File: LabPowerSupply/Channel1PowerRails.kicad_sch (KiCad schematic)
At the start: 11 parts

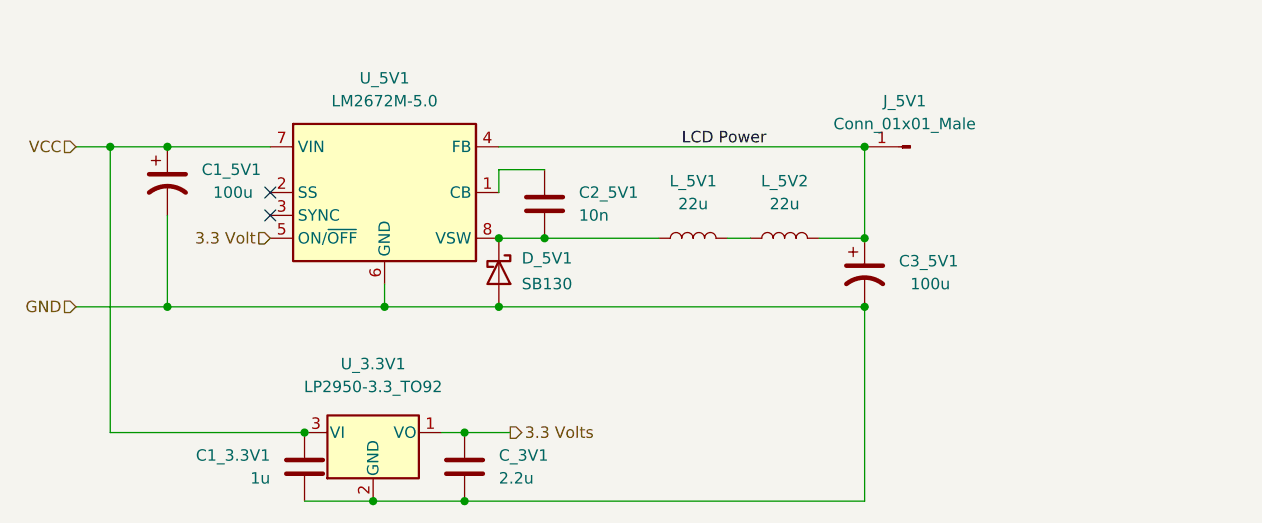
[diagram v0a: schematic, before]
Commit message: Changed most parts to smd
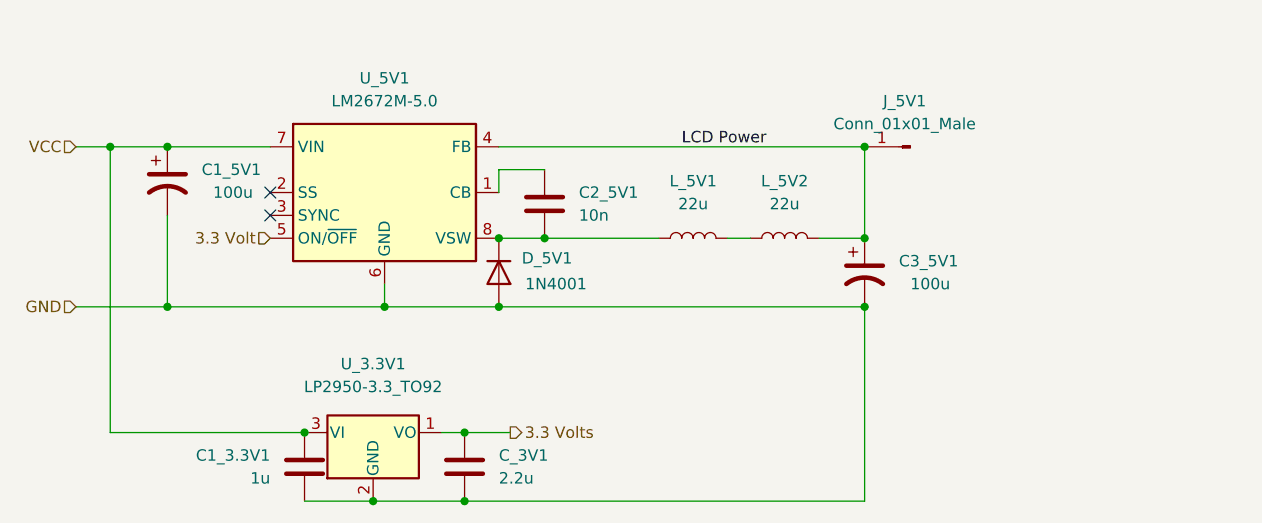
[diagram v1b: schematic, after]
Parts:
- C1_3.3V1, C_3V1: footprint Capacitor_THT:C_Disc_D5.0mm_W2.5mm_P2.50mm -> Capacitor_SMD:C_0805_2012Metric
- C2_5V1: footprint Capacitor_THT:C_Disc_D6.0mm_W2.5mm_P5.00mm -> Capacitor_SMD:C_0805_2012Metric
- D_5V1: value SB130 -> 1N4001; footprint Diode_THT:D_DO-41_SOD81_P10.16mm_Horizontal -> Diode_SMD:D_SMA; symbol Diode:SB130 -> Diode:1N4001
- U_3.3V1: footprint Package_TO_SOT_THT:TO-92_Inline -> Package_TO_SOT_SMD:TO-252-3_TabPin4
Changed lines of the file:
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@@
       (effects (font (size 1.27 1.27)) (justify left))
     )
-    (property "Footprint" "Capacitor_THT:C_Disc_D5.0mm_W2.5mm_P2.50mm" (id 2) (at 136.8552 128.27 0)
+    (property "Footprint" "Capacitor_SMD:C_0805_2012Metric" (id 2) (at 136.8552 128.27 0)
       (effects (font (size 1.27 1.27)) hide)
     )
@@
     (property "Reference" "U_3.3V1" (id 0) (at 125.73 113.03 0))
     (property "Value" "LP2950-3.3_TO92" (id 1) (at 125.73 115.57 0))
-    (property "Footprint" "Package_TO_SOT_THT:TO-92_Inline" (id 2) (at 125.73 114.935 0)
+    (property "Footprint" "Package_TO_SOT_SMD:TO-252-3_TabPin4" (id 2) (at 125.73 114.935 0)
       (effects (font (size 1.27 1.27) italic) hide)
     )
@@
       (effects (font (size 1.27 1.27)) (justify right))
     )
-    (property "Footprint" "Capacitor_THT:C_Disc_D5.0mm_W2.5mm_P2.50mm" (id 2) (at 119.0752 120.65 0)
+    (property "Footprint" "Capacitor_SMD:C_0805_2012Metric" (id 2) (at 119.0752 120.65 0)
       (effects (font (size 1.27 1.27)) hide)
     )
@@
     (pin "2")
   )
-  (symbol (lib_id "Diode:SB130") (at 139.7 102.87 270) (unit 1)
+  (symbol (lib_id "Diode:1N4001") (at 139.7 102.87 270) (unit 1)
     (in_bom yes) (on_board yes)
     (property "Reference" "D_5V1" (id 0) (at 142.24 101.2824 90)
       (effects (font (size 1.27 1.27)) (justify left))
     )
-    (property "Value" "SB130" (id 1) (at 142.24 104.14 90)
-      (effects (font (size 1.27 1.27)) (justify left))
-    )
-    (property "Footprint" "Diode_THT:D_DO-41_SOD81_P10.16mm_Horizontal" (id 2) (at 135.255 102.87 0)
+    (property "Value" "1N4001" (id 1) (at 146.05 104.14 90))
+    (property "Footprint" "Diode_SMD:D_SMA" (id 2) (at 135.255 102.87 0)
       (effects (font (size 1.27 1.27)) hide)
     )
-    (property "Datasheet" "http://www.diodes.com/_files/datasheets/ds23022.pdf" (id 3) (at 139.7 102.87 0)
+    (property "Datasheet" "http://www.vishay.com/docs/88503/1n4001.pdf" (id 3) (at 139.7 102.87 0)
       (effects (font (size 1.27 1.27)) hide)
     )
@@
       (effects (font (size 1.27 1.27)) (justify left))
     )
-    (property "Footprint" "Capacitor_THT:C_Disc_D6.0mm_W2.5mm_P5.00mm" (id 2) (at 145.7452 99.06 0)
+    (property "Footprint" "Capacitor_SMD:C_0805_2012Metric" (id 2) (at 145.7452 99.06 0)
       (effects (font (size 1.27 1.27)) hide)
     )

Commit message: Start tallying
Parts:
- removed D_5V1: 1N4001, Diode_SMD:D_SMA, symbol Diode:1N4001
- removed J_5V1: Conn_01x01_Male, Connector_PinHeader_2.54mm:PinHeader_1x01_P2.54mm_Vertical, symbol Connector:Conn_01x01_Male
- removed L_5V2: 22u, Inductor_THT:L_Radial_D6.0mm_P4.00mm, symbol Device:L
- removed U_5V1: LM2672M-5.0, Package_SO:SOIC-8_3.9x4.9mm_P1.27mm, symbol Regulator_Switching:LM2672M-5.0
- added U_5V1: AP63205WU, Package_TO_SOT_SMD:TSOT-23-6, symbol Regulator_Switching:AP63205WU
- C1_5V1: value 100u -> 10u; footprint Capacitor_THT:CP_Radial_D10.0mm_P5.00mm -> Capacitor_THT:CP_Radial_D8.0mm_P3.50mm
- C2_5V1: value 10n -> 100n; footprint Capacitor_SMD:C_0805_2012Metric -> Capacitor_SMD:C_0603_1608Metric
- C3_5V1: value 100u -> 68u; footprint Capacitor_THT:CP_Radial_D10.0mm_P5.00mm -> Capacitor_THT:CP_Radial_D8.0mm_P3.50mm
- L_5V1: value 22u -> 4.7u; footprint Inductor_THT:L_Radial_D6.0mm_P4.00mm -> Inductor_SMD:L_Sumida_CDMC6D28_7.25x6.5mm
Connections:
- net LCD Power is gone; now on net 5 Volts: C3_5V1.1
- net GND: now also U_5V1.4 (GND)
- net VCC: now also U_5V1.2 (EN), U_5V1.3 (IN)
- net at L_5V1.1: now also C2_5V1.1, U_5V1.5 (SW); no longer C2_5V1.2
- net 5 Volts: now reaches L_5V1.2
- net 5 Volts: now also U_5V1.1 (FB)
- new net: C2_5V1.2, U_5V1.6 (BST)
- no-connect marks 2 -> 0
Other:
- moved on the sheet: C1_3.3V1, C1_5V1, C3_5V1

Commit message: almost done
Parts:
- C1_3.3V1: footprint Capacitor_SMD:C_0805_2012Metric -> Capacitor_SMD:C_0603_1608Metric
- C1_5V1: value 10u -> 68u
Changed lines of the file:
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@@
       (effects (font (size 1.27 1.27)) (justify right))
     )
-    (property "Footprint" "Capacitor_SMD:C_0805_2012Metric" (id 2) (at 111.4552 120.65 0)
+    (property "Footprint" "Capacitor_SMD:C_0603_1608Metric" (id 2) (at 111.4552 120.65 0)
       (effects (font (size 1.27 1.27)) hide)
     )
@@
       (effects (font (size 1.27 1.27)) (justify left))
     )
-    (property "Value" "10u" (id 1) (at 107.95 101.6 0)
+    (property "Value" "68u" (id 1) (at 107.95 101.6 0)
       (effects (font (size 1.27 1.27)) (justify left))
     )

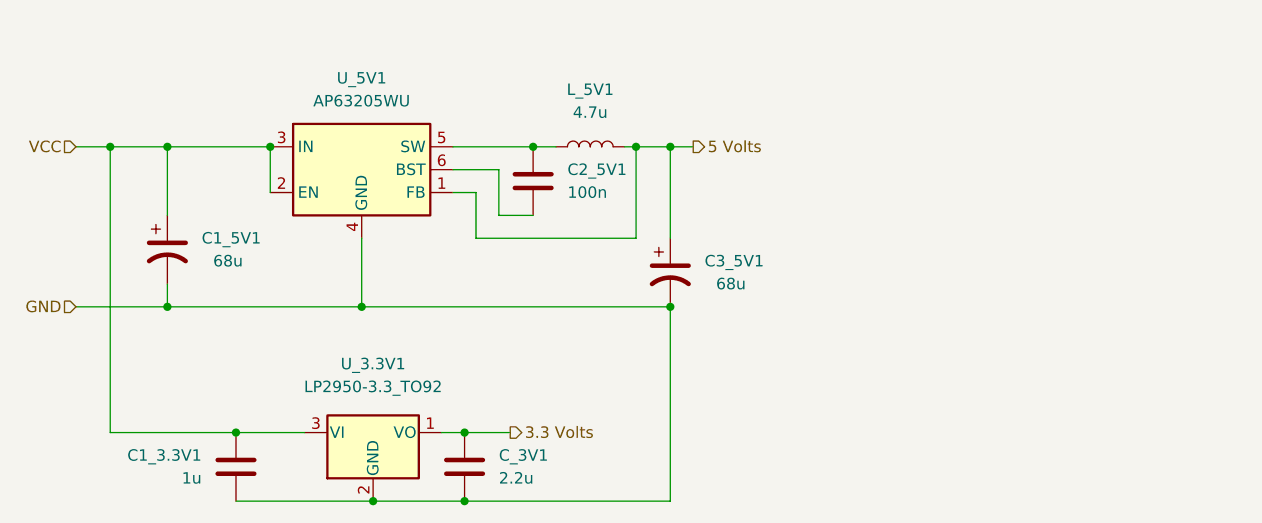
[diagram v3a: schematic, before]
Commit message: Pre regulate 3.3v
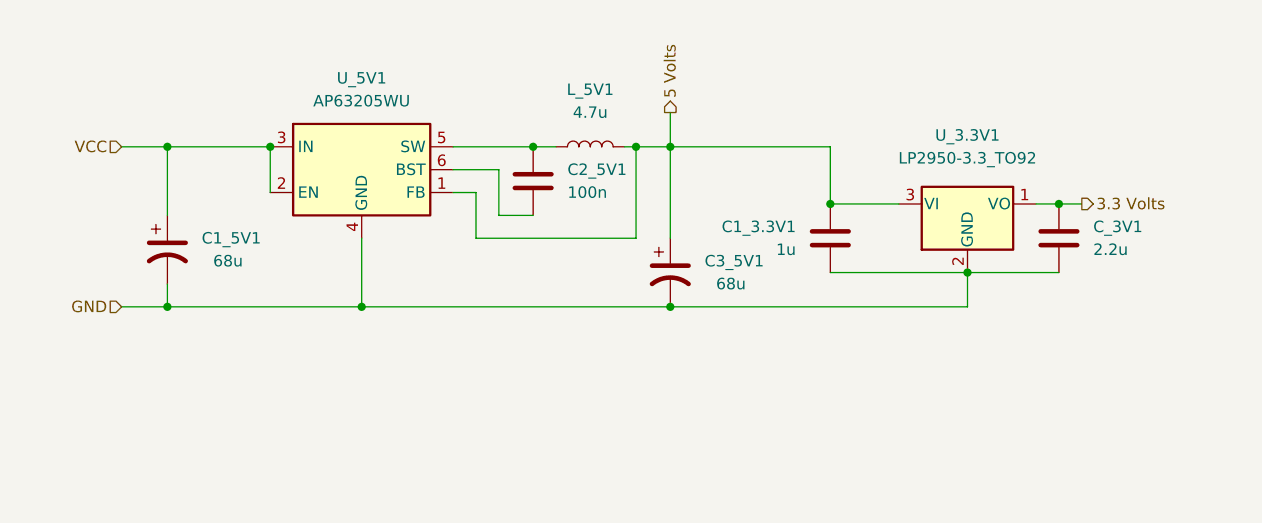
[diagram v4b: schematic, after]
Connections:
- net 5 Volts: now also C1_3.3V1.2, U_3.3V1.3 (VI)
- net VCC: no longer C1_3.3V1.2, U_3.3V1.3 (VI)
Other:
- moved on the sheet: C1_3.3V1, C_3V1, U_3.3V1
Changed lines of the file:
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@@
     (comment 4 "This supplys the 5 volts and 3.3 volts rail for the primary digital")
-  )
-  (junction (at 110.49 120.65) (diameter 0) (color 0 0 0 0)
   )
   (junction (at 102.87 106.68) (diameter 0) (color 0 0 0 0)
@@
   (junction (at 114.3 88.9) (diameter 0) (color 0 0 0 0)
   )
-  (junction (at 96.52 88.9) (diameter 0) (color 0 0 0 0)
-  )
-  (junction (at 135.89 128.27) (diameter 0) (color 0 0 0 0)
+  (junction (at 176.53 95.25) (diameter 0) (color 0 0 0 0)
   )
   (junction (at 158.75 106.68) (diameter 0) (color 0 0 0 0)
   )
+  (junction (at 124.46 106.68) (diameter 0) (color 0 0 0 0)
+  )
+  (junction (at 191.77 102.87) (diameter 0) (color 0 0 0 0)
+  )
   (junction (at 158.75 88.9) (diameter 0) (color 0 0 0 0)
   )
-  (junction (at 124.46 106.68) (diameter 0) (color 0 0 0 0)
-  )
-  (junction (at 125.73 128.27) (diameter 0) (color 0 0 0 0)
-  )
-  (junction (at 135.89 120.65) (diameter 0) (color 0 0 0 0)
+  (junction (at 201.93 95.25) (diameter 0) (color 0 0 0 0)
   )
   (junction (at 143.51 88.9) (diameter 0) (color 0 0 0 0)
@@
     (stroke (width 0) (type default) (color 0 0 0 0))
   )
-  (wire (pts (xy 92.71 88.9) (xy 96.52 88.9))
+  (wire (pts (xy 97.79 88.9) (xy 102.87 88.9))
     (stroke (width 0) (type default) (color 0 0 0 0))
   )
@@
     (stroke (width 0) (type default) (color 0 0 0 0))
   )
-  (wire (pts (xy 110.49 128.27) (xy 125.73 128.27))
+  (wire (pts (xy 201.93 95.25) (xy 204.47 95.25))
     (stroke (width 0) (type default) (color 0 0 0 0))
   )
-  (wire (pts (xy 158.75 128.27) (xy 158.75 106.68))
+  (wire (pts (xy 176.53 102.87) (xy 191.77 102.87))
     (stroke (width 0) (type default) (color 0 0 0 0))
   )
-  (wire (pts (xy 96.52 120.65) (xy 110.49 120.65))
+  (wire (pts (xy 176.53 88.9) (xy 176.53 95.25))
     (stroke (width 0) (type default) (color 0 0 0 0))
   )
@@
     (stroke (width 0) (type default) (color 0 0 0 0))
   )
-  (wire (pts (xy 134.62 88.9) (xy 143.51 88.9))
+  (wire (pts (xy 158.75 88.9) (xy 176.53 88.9))
     (stroke (width 0) (type default) (color 0 0 0 0))
   )
-  (wire (pts (xy 96.52 120.65) (xy 96.52 88.9))
+  (wire (pts (xy 134.62 88.9) (xy 143.51 88.9))
     (stroke (width 0) (type default) (color 0 0 0 0))
   )
@@
     (stroke (width 0) (type default) (color 0 0 0 0))
   )
-  (wire (pts (xy 139.7 91.44) (xy 134.62 91.44))
+  (wire (pts (xy 158.75 85.09) (xy 158.75 88.9))
     (stroke (width 0) (type default) (color 0 0 0 0))
   )
-  (wire (pts (xy 135.89 128.27) (xy 158.75 128.27))
-    (stroke (width 0) (type default) (color 0 0 0 0))
-  )
-  (wire (pts (xy 158.75 88.9) (xy 161.29 88.9))
+  (wire (pts (xy 139.7 91.44) (xy 134.62 91.44))
     (stroke (width 0) (type default) (color 0 0 0 0))
   )
@@
     (stroke (width 0) (type default) (color 0 0 0 0))
   )
-  (wire (pts (xy 96.52 88.9) (xy 102.87 88.9))
+  (wire (pts (xy 158.75 106.68) (xy 191.77 106.68))
     (stroke (width 0) (type default) (color 0 0 0 0))
   )
@@
     (stroke (width 0) (type default) (color 0 0 0 0))
   )
-  (wire (pts (xy 110.49 120.65) (xy 118.11 120.65))
+  (wire (pts (xy 176.53 95.25) (xy 184.15 95.25))
     (stroke (width 0) (type default) (color 0 0 0 0))
   )
@@
     (stroke (width 0) (type default) (color 0 0 0 0))
   )
-  (wire (pts (xy 92.71 106.68) (xy 102.87 106.68))
+  (wire (pts (xy 191.77 106.68) (xy 191.77 102.87))
+    (stroke (width 0) (type default) (color 0 0 0 0))
+  )
+  (wire (pts (xy 97.79 106.68) (xy 102.87 106.68))
     (stroke (width 0) (type default) (color 0 0 0 0))
   )
@@
     (stroke (width 0) (type default) (color 0 0 0 0))
   )
-  (wire (pts (xy 125.73 128.27) (xy 135.89 128.27))
+  (wire (pts (xy 191.77 102.87) (xy 201.93 102.87))
     (stroke (width 0) (type default) (color 0 0 0 0))
   )
@@
     (stroke (width 0) (type default) (color 0 0 0 0))
   )
-  (wire (pts (xy 135.89 120.65) (xy 140.97 120.65))
-    (stroke (width 0) (type default) (color 0 0 0 0))
-  )
   (wire (pts (xy 102.87 106.68) (xy 124.46 106.68))
     (stroke (width 0) (type default) (color 0 0 0 0))
   )
-  (wire (pts (xy 133.35 120.65) (xy 135.89 120.65))
+  (wire (pts (xy 199.39 95.25) (xy 201.93 95.25))
     (stroke (width 0) (type default) (color 0 0 0 0))
   )
@@
     (stroke (width 0) (type default) (color 0 0 0 0))
   )
-  (hierarchical_label "GND" (shape input) (at 92.71 106.68 180)
+  (hierarchical_label "GND" (shape input) (at 97.79 106.68 180)
     (effects (font (size 1.27 1.27)) (justify right))
   )
-  (hierarchical_label "3.3 Volts" (shape output) (at 140.97 120.65 0)
+  (hierarchical_label "3.3 Volts" (shape output) (at 204.47 95.25 0)
     (effects (font (size 1.27 1.27)) (justify left))
   )
-  (hierarchical_label "VCC" (shape input) (at 92.71 88.9 180)
+  (hierarchical_label "VCC" (shape input) (at 97.79 88.9 180)
     (effects (font (size 1.27 1.27)) (justify right))
   )
-  (hierarchical_label "5 Volts" (shape output) (at 161.29 88.9 0)
+  (hierarchical_label "5 Volts" (shape output) (at 158.75 85.09 90)
     (effects (font (size 1.27 1.27)) (justify left))
   )
-  (symbol (lib_id "Device:C") (at 135.89 124.46 0) (unit 1)
+  (symbol (lib_id "Device:C") (at 201.93 99.06 0) (unit 1)
     (in_bom yes) (on_board yes) (fields_autoplaced)
-    (property "Reference" "C_3V1" (id 0) (at 139.7 123.1899 0)
+    (property "Reference" "C_3V1" (id 0) (at 205.74 97.7899 0)
       (effects (font (size 1.27 1.27)) (justify left))
     )
-    (property "Value" "2.2u" (id 1) (at 139.7 125.7299 0)
+    (property "Value" "2.2u" (id 1) (at 205.74 100.3299 0)
       (effects (font (size 1.27 1.27)) (justify left))
     )
-    (property "Footprint" "Capacitor_SMD:C_0805_2012Metric" (id 2) (at 136.8552 128.27 0)
+    (property "Footprint" "Capacitor_SMD:C_0805_2012Metric" (id 2) (at 202.8952 102.87 0)
       (effects (font (size 1.27 1.27)) hide)
     )
-    (property "Datasheet" "~" (id 3) (at 135.89 124.46 0)
+    (property "Datasheet" "~" (id 3) (at 201.93 99.06 0)
       (effects (font (size 1.27 1.27)) hide)
     )
@@
     (pin "2")
   )
-  (symbol (lib_id "Regulator_Linear:LP2950-3.3_TO92") (at 125.73 120.65 0) (unit 1)
+  (symbol (lib_id "Regulator_Linear:LP2950-3.3_TO92") (at 191.77 95.25 0) (unit 1)
     (in_bom yes) (on_board yes) (fields_autoplaced)
-    (property "Reference" "U_3.3V1" (id 0) (at 125.73 113.03 0))
-    (property "Value" "LP2950-3.3_TO92" (id 1) (at 125.73 115.57 0))
-    (property "Footprint" "Package_TO_SOT_SMD:TO-252-3_TabPin4" (id 2) (at 125.73 114.935 0)
+    (property "Reference" "U_3.3V1" (id 0) (at 191.77 87.63 0))
+    (property "Value" "LP2950-3.3_TO92" (id 1) (at 191.77 90.17 0))
+    (property "Footprint" "Package_TO_SOT_SMD:TO-252-3_TabPin4" (id 2) (at 191.77 89.535 0)
       (effects (font (size 1.27 1.27) italic) hide)
     )
-    (property "Datasheet" "http://www.ti.com/lit/ds/symlink/lp2950.pdf" (id 3) (at 125.73 121.92 0)
+    (property "Datasheet" "http://www.ti.com/lit/ds/symlink/lp2950.pdf" (id 3) (at 191.77 96.52 0)
       (effects (font (size 1.27 1.27)) hide)
     )
@@
     (pin "3")
   )
-  (symbol (lib_id "Device:C") (at 110.49 124.46 0) (mirror x) (unit 1)
+  (symbol (lib_id "Device:C") (at 176.53 99.06 0) (mirror x) (unit 1)
     (in_bom yes) (on_board yes) (fields_autoplaced)
-    (property "Reference" "C1_3.3V1" (id 0) (at 106.68 123.1899 0)
+    (property "Reference" "C1_3.3V1" (id 0) (at 172.72 97.7899 0)
       (effects (font (size 1.27 1.27)) (justify right))
     )
-    (property "Value" "1u" (id 1) (at 106.68 125.7299 0)
+    (property "Value" "1u" (id 1) (at 172.72 100.3299 0)
       (effects (font (size 1.27 1.27)) (justify right))
     )
-    (property "Footprint" "Capacitor_SMD:C_0603_1608Metric" (id 2) (at 111.4552 120.65 0)
+    (property "Footprint" "Capacitor_SMD:C_0603_1608Metric" (id 2) (at 177.4952 95.25 0)
       (effects (font (size 1.27 1.27)) hide)
     )
-    (property "Datasheet" "~" (id 3) (at 110.49 124.46 0)
+    (property "Datasheet" "~" (id 3) (at 176.53 99.06 0)
       (effects (font (size 1.27 1.27)) hide)
     )

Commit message: Changed capacitors to x7r
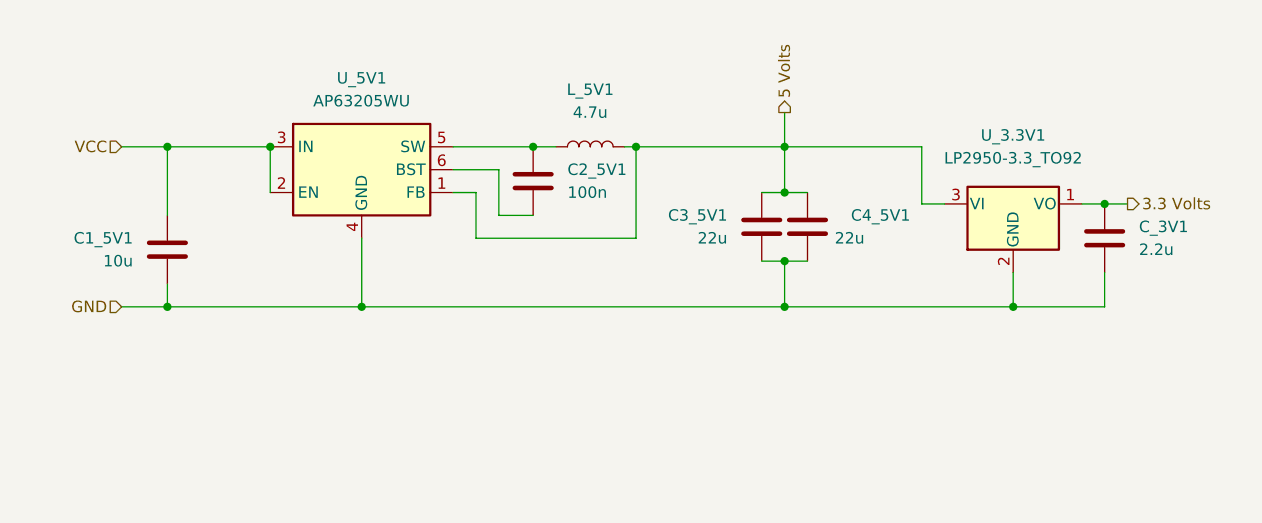
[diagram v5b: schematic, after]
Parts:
- removed C1_3.3V1: 1u, Capacitor_SMD:C_0603_1608Metric, symbol Device:C
- removed C1_5V1, C3_5V1: 68u, Capacitor_THT:CP_Radial_D8.0mm_P3.50mm, symbol Device:C_Polarized_US
- added C1_5V1: 10u, Capacitor_SMD:C_1210_3225Metric, symbol Device:C
- added C3_5V1, C4_5V1: 22u, Capacitor_SMD:C_1210_3225Metric, symbol Device:C
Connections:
- net 5 Volts: now also C3_5V1.2, C4_5V1.2
- net GND: now also C1_5V1.1, C3_5V1.1, C4_5V1.1
- net VCC: now also C1_5V1.2
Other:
- moved on the sheet: C_3V1, U_3.3V1

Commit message: Fixed cap footprints
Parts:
- C1_5V1: footprint Capacitor_SMD:C_1210_3225Metric -> Capacitor_SMD:C_1206_3216Metric
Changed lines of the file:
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@@
       (effects (font (size 1.27 1.27)) (justify right))
     )
-    (property "Footprint" "Capacitor_SMD:C_1210_3225Metric" (id 2) (at 103.8352 96.52 0)
+    (property "Footprint" "Capacitor_SMD:C_1206_3216Metric" (id 2) (at 103.8352 96.52 0)
       (effects (font (size 1.27 1.27)) hide)
     )
